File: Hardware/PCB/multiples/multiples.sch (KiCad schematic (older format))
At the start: 31 parts, among them J1 AudioJack2_SwitchT, J10 AudioJack2, J11 AudioJack2, J2 Synth_power_2x5, J3 AudioJack2, J4 AudioJack2, J5 AudioJack2, J6 AudioJack2, J7 AudioJack2_SwitchT, J8 AudioJack2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

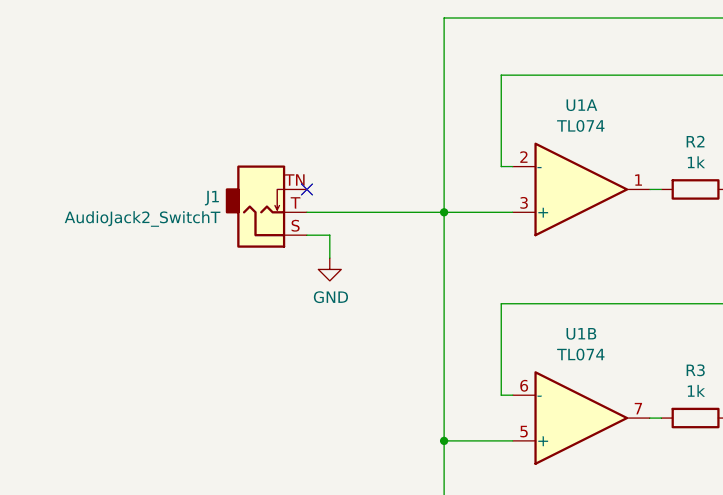
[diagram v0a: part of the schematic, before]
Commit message: Footprints, ground tip normal
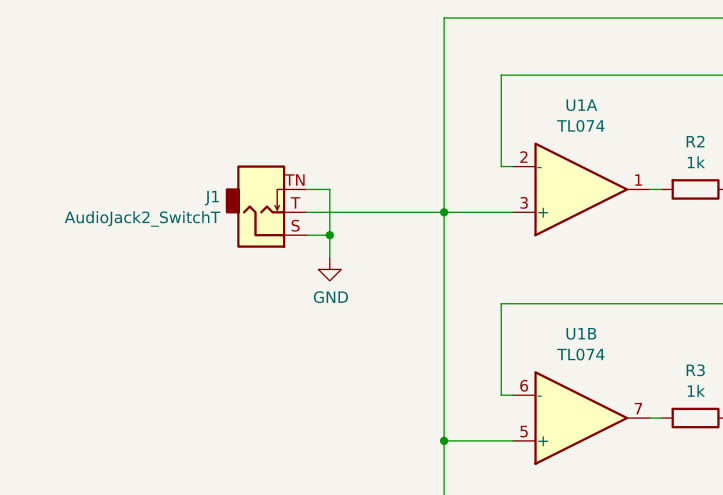
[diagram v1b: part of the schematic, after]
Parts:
- J1, J10, J11, J3, J4, J5, J6, J7, J8, J9: footprint (none) -> ao_tht:Jack_6.35mm_PJ_629HAN
- R1, R10, R2, R3, R4, R5, R6, R7, R8, R9: footprint (none) -> ao_tht:R_Axial_DIN0207_L6.3mm_D2.5mm_P10.16mm_Horizontal
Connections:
- net GND: now also J1.TN
- no-connect marks 1 -> 0
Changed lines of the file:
@@
 F 0 "R2" V 3393 1750 50  0000 C CNN
 F 1 "1k" V 3484 1750 50  0000 C CNN
-F 2 "" V 3530 1750 50  0001 C CNN
+F 2 "ao_tht:R_Axial_DIN0207_L6.3mm_D2.5mm_P10.16mm_Horizontal" V 3530 1750 50  0001 C CNN
 F 3 "~" H 3600 1750 50  0001 C CNN
 	1    3600 1750
@@
 F 0 "J1" H 1521 1783 50  0000 R CNN
 F 1 "AudioJack2_SwitchT" H 1521 1874 50  0000 R CNN
-F 2 "" H 1700 1850 50  0001 C CNN
+F 2 "ao_tht:Jack_6.35mm_PJ_629HAN" H 1700 1850 50  0001 C CNN
 F 3 "~" H 1700 1850 50  0001 C CNN
 	1    1700 1850
@@
 F 0 "J3" H 4270 1733 50  0000 R CNN
 F 1 "AudioJack2" H 4270 1824 50  0000 R CNN
-F 2 "" H 4450 1750 50  0001 C CNN
+F 2 "ao_tht:Jack_6.35mm_PJ_629HAN" H 4450 1750 50  0001 C CNN
 F 3 "~" H 4450 1750 50  0001 C CNN
 	1    4450 1750
@@
 F 0 "R3" V 3393 2750 50  0000 C CNN
 F 1 "1k" V 3484 2750 50  0000 C CNN
-F 2 "" V 3530 2750 50  0001 C CNN
+F 2 "ao_tht:R_Axial_DIN0207_L6.3mm_D2.5mm_P10.16mm_Horizontal" V 3530 2750 50  0001 C CNN
 F 3 "~" H 3600 2750 50  0001 C CNN
 	1    3600 2750
@@
 F 0 "J4" H 4270 2733 50  0000 R CNN
 F 1 "AudioJack2" H 4270 2824 50  0000 R CNN
-F 2 "" H 4450 2750 50  0001 C CNN
+F 2 "ao_tht:Jack_6.35mm_PJ_629HAN" H 4450 2750 50  0001 C CNN
 F 3 "~" H 4450 2750 50  0001 C CNN
 	1    4450 2750
@@
 F 0 "R4" V 3393 3750 50  0000 C CNN
 F 1 "1k" V 3484 3750 50  0000 C CNN
-F 2 "" V 3530 3750 50  0001 C CNN
+F 2 "ao_tht:R_Axial_DIN0207_L6.3mm_D2.5mm_P10.16mm_Horizontal" V 3530 3750 50  0001 C CNN
 F 3 "~" H 3600 3750 50  0001 C CNN
 	1    3600 3750
@@
 F 0 "J5" H 4270 3733 50  0000 R CNN
 F 1 "AudioJack2" H 4270 3824 50  0000 R CNN
-F 2 "" H 4450 3750 50  0001 C CNN
+F 2 "ao_tht:Jack_6.35mm_PJ_629HAN" H 4450 3750 50  0001 C CNN
 F 3 "~" H 4450 3750 50  0001 C CNN
 	1    4450 3750
@@
 F 0 "R5" V 3393 4750 50  0000 C CNN
 F 1 "1k" V 3484 4750 50  0000 C CNN
-F 2 "" V 3530 4750 50  0001 C CNN
+F 2 "ao_tht:R_Axial_DIN0207_L6.3mm_D2.5mm_P10.16mm_Horizontal" V 3530 4750 50  0001 C CNN
 F 3 "~" H 3600 4750 50  0001 C CNN
 	1    3600 4750
@@
 F 0 "J6" H 4270 4733 50  0000 R CNN
 F 1 "AudioJack2" H 4270 4824 50  0000 R CNN
-F 2 "" H 4450 4750 50  0001 C CNN
+F 2 "ao_tht:Jack_6.35mm_PJ_629HAN" H 4450 4750 50  0001 C CNN
 F 3 "~" H 4450 4750 50  0001 C CNN
 	1    4450 4750
@@
 	1    0    0    -1
 $EndComp
-NoConn ~ 1900 1750
 $Comp
 L ao_symbols:TL074 U2
@@
 F 0 "R7" V 7893 1750 50  0000 C CNN
 F 1 "1k" V 7984 1750 50  0000 C CNN
-F 2 "" V 8030 1750 50  0001 C CNN
+F 2 "ao_tht:R_Axial_DIN0207_L6.3mm_D2.5mm_P10.16mm_Horizontal" V 8030 1750 50  0001 C CNN
 F 3 "~" H 8100 1750 50  0001 C CNN
 	1    8100 1750
@@
 F 0 "J7" H 6021 1783 50  0000 R CNN
 F 1 "AudioJack2_SwitchT" H 6021 1874 50  0000 R CNN
-F 2 "" H 6200 1850 50  0001 C CNN
+F 2 "ao_tht:Jack_6.35mm_PJ_629HAN" H 6200 1850 50  0001 C CNN
 F 3 "~" H 6200 1850 50  0001 C CNN
 	1    6200 1850
@@
 F 0 "J8" H 8770 1733 50  0000 R CNN
 F 1 "AudioJack2" H 8770 1824 50  0000 R CNN
-F 2 "" H 8950 1750 50  0001 C CNN
+F 2 "ao_tht:Jack_6.35mm_PJ_629HAN" H 8950 1750 50  0001 C CNN
 F 3 "~" H 8950 1750 50  0001 C CNN
 	1    8950 1750
@@
 F 0 "R8" V 7893 2750 50  0000 C CNN
 F 1 "1k" V 7984 2750 50  0000 C CNN
-F 2 "" V 8030 2750 50  0001 C CNN
+F 2 "ao_tht:R_Axial_DIN0207_L6.3mm_D2.5mm_P10.16mm_Horizontal" V 8030 2750 50  0001 C CNN
 F 3 "~" H 8100 2750 50  0001 C CNN
 	1    8100 2750
@@
 F 0 "J9" H 8770 2733 50  0000 R CNN
 F 1 "AudioJack2" H 8770 2824 50  0000 R CNN
-F 2 "" H 8950 2750 50  0001 C CNN
+F 2 "ao_tht:Jack_6.35mm_PJ_629HAN" H 8950 2750 50  0001 C CNN
 F 3 "~" H 8950 2750 50  0001 C CNN
 	1    8950 2750
@@
 F 0 "R9" V 7893 3750 50  0000 C CNN
 F 1 "1k" V 7984 3750 50  0000 C CNN
-F 2 "" V 8030 3750 50  0001 C CNN
+F 2 "ao_tht:R_Axial_DIN0207_L6.3mm_D2.5mm_P10.16mm_Horizontal" V 8030 3750 50  0001 C CNN
 F 3 "~" H 8100 3750 50  0001 C CNN
 	1    8100 3750
@@
 F 0 "J10" H 8770 3733 50  0000 R CNN
 F 1 "AudioJack2" H 8770 3824 50  0000 R CNN
-F 2 "" H 8950 3750 50  0001 C CNN
+F 2 "ao_tht:Jack_6.35mm_PJ_629HAN" H 8950 3750 50  0001 C CNN
 F 3 "~" H 8950 3750 50  0001 C CNN
 	1    8950 3750
@@
 F 0 "R10" V 7893 4750 50  0000 C CNN
 F 1 "1k" V 7984 4750 50  0000 C CNN
-F 2 "" V 8030 4750 50  0001 C CNN
+F 2 "ao_tht:R_Axial_DIN0207_L6.3mm_D2.5mm_P10.16mm_Horizontal" V 8030 4750 50  0001 C CNN
 F 3 "~" H 8100 4750 50  0001 C CNN
 	1    8100 4750
@@
 F 0 "J11" H 8770 4733 50  0000 R CNN
 F 1 "AudioJack2" H 8770 4824 50  0000 R CNN
-F 2 "" H 8950 4750 50  0001 C CNN
+F 2 "ao_tht:Jack_6.35mm_PJ_629HAN" H 8950 4750 50  0001 C CNN
 F 3 "~" H 8950 4750 50  0001 C CNN
 	1    8950 4750
@@
 F 0 "R1" H 2570 5146 50  0000 L CNN
 F 1 "1M" H 2570 5055 50  0000 L CNN
-F 2 "" V 2430 5100 50  0001 C CNN
+F 2 "ao_tht:R_Axial_DIN0207_L6.3mm_D2.5mm_P10.16mm_Horizontal" V 2430 5100 50  0001 C CNN
 F 3 "~" H 2500 5100 50  0001 C CNN
 	1    2500 5100
@@
 F 0 "R6" H 7070 5146 50  0000 L CNN
 F 1 "1M" H 7070 5055 50  0000 L CNN
-F 2 "" V 6930 5100 50  0001 C CNN
+F 2 "ao_tht:R_Axial_DIN0207_L6.3mm_D2.5mm_P10.16mm_Horizontal" V 6930 5100 50  0001 C CNN
 F 3 "~" H 7000 5100 50  0001 C CNN
 	1    7000 5100
@@
 	7000 4950 7000 4850
 Connection ~ 7000 4850
+Wire Wire Line
+	1900 1750 2000 1750
+Wire Wire Line
+	2000 1750 2000 1950
+Connection ~ 2000 1950
 $EndSCHEMATC

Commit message: PCB layout
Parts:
- added GRAF1: Holes, multiples:multiples_panel_holes, symbol ao_symbols:Graphic
- added GRAF2: AO logo, ao_tht:analogoutput, symbol ao_symbols:Graphic
- added GRAF3: CC0 logo, ao_tht:CC0_logo, symbol ao_symbols:Graphic
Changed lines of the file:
@@
 	2000 1750 2000 1950
 Connection ~ 2000 1950
+$Comp
+L ao_symbols:Graphic GRAF1
+U 1 1 611C08DC
+P 6750 6100
+F 0 "GRAF1" H 7028 6146 50  0000 L CNN
+F 1 "Holes" H 7028 6055 50  0000 L CNN
+F 2 "multiples:multiples_panel_holes" H 6750 6100 50  0001 C CNN
+F 3 "" H 6750 6100 50  0001 C CNN
+F 4 "DNF" H 6750 6100 50  0001 C CNN "Config"
+	1    6750 6100
+	1    0    0    -1
+$EndComp
+$Comp
+L ao_symbols:Graphic GRAF2
+U 1 1 611C0DA7
+P 7750 6100
+F 0 "GRAF2" H 8028 6146 50  0000 L CNN
+F 1 "AO logo" H 8028 6055 50  0000 L CNN
+F 2 "ao_tht:analogoutput" H 7750 6100 50  0001 C CNN
+F 3 "" H 7750 6100 50  0001 C CNN
+F 4 "DNF" H 7750 6100 50  0001 C CNN "Config"
+	1    7750 6100
+	1    0    0    -1
+$EndComp
+$Comp
+L ao_symbols:Graphic GRAF3
+U 1 1 611C1098
+P 8750 6100
+F 0 "GRAF3" H 9028 6146 50  0000 L CNN
+F 1 "CC0 logo" H 9028 6055 50  0000 L CNN
+F 2 "ao_tht:CC0_logo" H 8750 6100 50  0001 C CNN
+F 3 "" H 8750 6100 50  0001 C CNN
+F 4 "DNF" H 8750 6100 50  0001 C CNN "Config"
+	1    8750 6100
+	1    0    0    -1
+$EndComp
 $EndSCHEMATC

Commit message: Clean up libraries, Schottky footprint update
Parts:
- D1, D2: footprint ao_tht:D_DO-41_SOD81_P7.62mm_Horizontal -> ao_tht:D_DO-41_SOD81_P10.16mm_Horizontal
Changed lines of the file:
@@
 F 0 "D1" H 2600 6634 50  0000 C CNN
 F 1 "1N5817" H 2600 6725 50  0000 C CNN
-F 2 "ao_tht:D_DO-41_SOD81_P7.62mm_Horizontal" H 2600 6850 50  0001 C CNN
+F 2 "ao_tht:D_DO-41_SOD81_P10.16mm_Horizontal" H 2600 6850 50  0001 C CNN
 F 3 "~" H 2600 6850 50  0001 C CNN
 F 4 "Tayda" H 2600 6850 50  0001 C CNN "Vendor"
@@
 F 0 "D2" H 2600 7034 50  0000 C CNN
 F 1 "1N5817" H 2600 7125 50  0000 C CNN
-F 2 "ao_tht:D_DO-41_SOD81_P7.62mm_Horizontal" H 2600 7250 50  0001 C CNN
+F 2 "ao_tht:D_DO-41_SOD81_P10.16mm_Horizontal" H 2600 7250 50  0001 C CNN
 F 3 "~" H 2600 7250 50  0001 C CNN
 F 4 "Tayda" H 2600 7250 50  0001 C CNN "Vendor"
